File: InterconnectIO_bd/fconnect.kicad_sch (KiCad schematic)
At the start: 191 parts, among them J1 9001-11961C00A, J2 9001-11961C00A, J3 7760, J4 7760

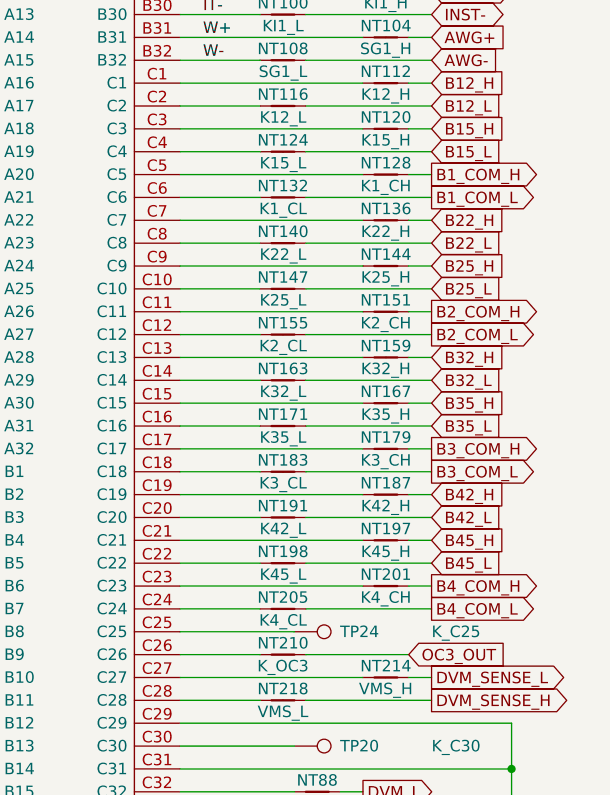
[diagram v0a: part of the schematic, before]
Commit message: Reverse COM_H and COM_L on relay Bank
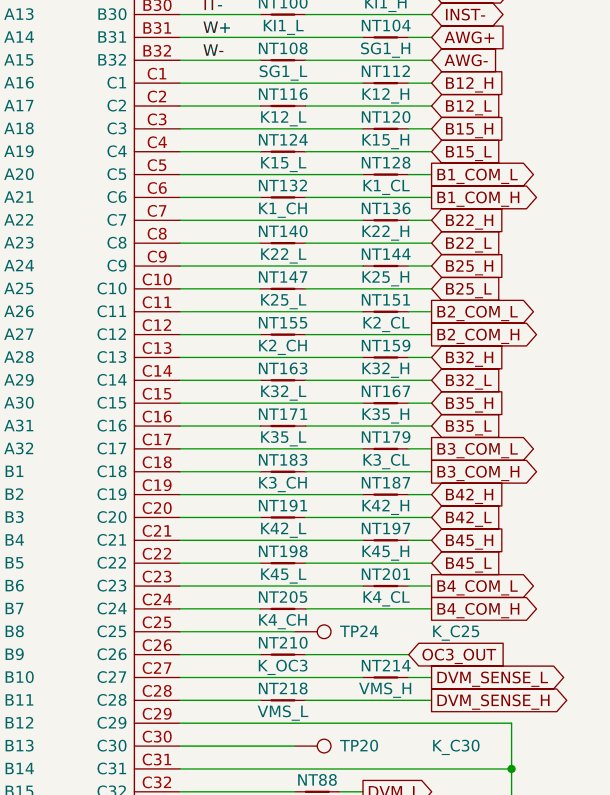
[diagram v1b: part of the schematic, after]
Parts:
- NT128: value K1_CH -> K1_CL
- NT132: value K1_CL -> K1_CH
- NT151: value K2_CH -> K2_CL
- NT155: value K2_CL -> K2_CH
- NT179: value K3_CH -> K3_CL
- NT183: value K3_CL -> K3_CH
- NT201: value K4_CH -> K4_CL
- NT205: value K4_CL -> K4_CH
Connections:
- net B1_COM_H: now also NT132.1; no longer NT128.1
- net B1_COM_L: now also NT128.1; no longer NT132.1
- net B2_COM_H: now also NT155.1; no longer NT151.1
- net B2_COM_L: now also NT151.1; no longer NT155.1
- net B3_COM_H: now also NT183.2; no longer NT179.2
- net B3_COM_L: now also NT179.2; no longer NT183.2
- net B4_COM_H: now also NT205.1; no longer NT201.1
- net B4_COM_L: now also NT201.1; no longer NT205.1
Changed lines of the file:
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@@
     )
   )
-  (global_label "B4_COM_L" (shape output) (at 241.3 133.35 0) (fields_autoplaced)
+  (global_label "B4_COM_H" (shape output) (at 241.3 133.35 0) (fields_autoplaced)
     (effects (font (size 1.27 1.27)) (justify left))
-    (property "Intersheetrefs" "${INTERSHEET_REFS}" (at 253.2079 133.2706 0)
+    (property "Intersheetrefs" "${INTERSHEET_REFS}" (at 254.0029 133.35 0)
       (effects (font (size 1.27 1.27)) (justify left) hide)
     )
@@
     )
   )
-  (global_label "B3_COM_L" (shape output) (at 241.3 118.11 0) (fields_autoplaced)
+  (global_label "B3_COM_H" (shape output) (at 241.3 118.11 0) (fields_autoplaced)
     (effects (font (size 1.27 1.27)) (justify left))
-    (property "Intersheetrefs" "${INTERSHEET_REFS}" (at 253.2079 118.0306 0)
+    (property "Intersheetrefs" "${INTERSHEET_REFS}" (at 254.0029 118.11 0)
       (effects (font (size 1.27 1.27)) (justify left) hide)
     )
@@
     )
   )
-  (global_label "B4_COM_H" (shape output) (at 241.3 130.81 0) (fields_autoplaced)
+  (global_label "B4_COM_L" (shape output) (at 241.3 130.81 0) (fields_autoplaced)
     (effects (font (size 1.27 1.27)) (justify left))
-    (property "Intersheetrefs" "${INTERSHEET_REFS}" (at 253.5102 130.7306 0)
+    (property "Intersheetrefs" "${INTERSHEET_REFS}" (at 253.7005 130.81 0)
       (effects (font (size 1.27 1.27)) (justify left) hide)
     )
@@
     )
   )
-  (global_label "B3_COM_H" (shape output) (at 241.3 115.57 0) (fields_autoplaced)
+  (global_label "B3_COM_L" (shape output) (at 241.3 115.57 0) (fields_autoplaced)
     (effects (font (size 1.27 1.27)) (justify left))
-    (property "Intersheetrefs" "${INTERSHEET_REFS}" (at 253.5102 115.4906 0)
+    (property "Intersheetrefs" "${INTERSHEET_REFS}" (at 253.7005 115.57 0)
       (effects (font (size 1.27 1.27)) (justify left) hide)
     )
@@
     )
   )
-  (global_label "B2_COM_L" (shape output) (at 241.3 102.87 0) (fields_autoplaced)
+  (global_label "B2_COM_H" (shape output) (at 241.3 102.87 0) (fields_autoplaced)
     (effects (font (size 1.27 1.27)) (justify left))
-    (property "Intersheetrefs" "${INTERSHEET_REFS}" (at 253.2079 102.7906 0)
+    (property "Intersheetrefs" "${INTERSHEET_REFS}" (at 254.0029 102.87 0)
       (effects (font (size 1.27 1.27)) (justify left) hide)
     )
@@
     )
   )
-  (global_label "B2_COM_H" (shape output) (at 241.3 100.33 0) (fields_autoplaced)
+  (global_label "B2_COM_L" (shape output) (at 241.3 100.33 0) (fields_autoplaced)
     (effects (font (size 1.27 1.27)) (justify left))
-    (property "Intersheetrefs" "${INTERSHEET_REFS}" (at 253.5102 100.2506 0)
+    (property "Intersheetrefs" "${INTERSHEET_REFS}" (at 253.7005 100.33 0)
       (effects (font (size 1.27 1.27)) (justify left) hide)
     )
@@
     )
   )
-  (global_label "B1_COM_L" (shape output) (at 241.3 87.63 0) (fields_autoplaced)
+  (global_label "B1_COM_H" (shape output) (at 241.3 87.63 0) (fields_autoplaced)
     (effects (font (size 1.27 1.27)) (justify left))
-    (property "Intersheetrefs" "${INTERSHEET_REFS}" (at 253.2079 87.5506 0)
+    (property "Intersheetrefs" "${INTERSHEET_REFS}" (at 254.0029 87.63 0)
       (effects (font (size 1.27 1.27)) (justify left) hide)
     )
@@
     )
   )
-  (global_label "B1_COM_H" (shape output) (at 241.3 85.09 0) (fields_autoplaced)
+  (global_label "B1_COM_L" (shape output) (at 241.3 85.09 0) (fields_autoplaced)
     (effects (font (size 1.27 1.27)) (justify left))
-    (property "Intersheetrefs" "${INTERSHEET_REFS}" (at 253.5102 85.0106 0)
+    (property "Intersheetrefs" "${INTERSHEET_REFS}" (at 253.7005 85.09 0)
       (effects (font (size 1.27 1.27)) (justify left) hide)
     )
@@
       (effects (font (size 1.27 1.27)))
     )
-    (property "Value" "K2_CH" (at 236.22 101.6 0)
+    (property "Value" "K2_CL" (at 236.22 101.6 0)
       (effects (font (size 1.27 1.27)))
     )
@@
       (effects (font (size 1.27 1.27)))
     )
-    (property "Value" "K1_CH" (at 236.22 86.36 0)
+    (property "Value" "K1_CL" (at 236.22 86.36 0)
       (effects (font (size 1.27 1.27)))
     )
@@
       (effects (font (size 1.27 1.27)))
     )
-    (property "Value" "K1_CL" (at 224.79 88.9 0)
+    (property "Value" "K1_CH" (at 224.79 88.9 0)
       (effects (font (size 1.27 1.27)))
     )
@@
       (effects (font (size 1.27 1.27)))
     )
-    (property "Value" "K2_CL" (at 224.79 104.14 0)
+    (property "Value" "K2_CH" (at 224.79 104.14 0)
       (effects (font (size 1.27 1.27)))
     )
@@
       (effects (font (size 1.27 1.27)))
     )
-    (property "Value" "K3_CL" (at 224.79 119.38 0)
+    (property "Value" "K3_CH" (at 224.79 119.38 0)
       (effects (font (size 1.27 1.27)))
     )
@@
       (effects (font (size 1.27 1.27)))
     )
-    (property "Value" "K4_CL" (at 224.79 134.62 0)
+    (property "Value" "K4_CH" (at 224.79 134.62 0)
       (effects (font (size 1.27 1.27)))
     )
@@
       (effects (font (size 1.27 1.27)))
     )
-    (property "Value" "K4_CH" (at 236.22 132.08 0)
+    (property "Value" "K4_CL" (at 236.22 132.08 0)
       (effects (font (size 1.27 1.27)))
     )
@@
       (effects (font (size 1.27 1.27)))
     )
-    (property "Value" "K3_CH" (at 236.22 116.84 0)
+    (property "Value" "K3_CL" (at 236.22 116.84 0)
       (effects (font (size 1.27 1.27)))
     )
